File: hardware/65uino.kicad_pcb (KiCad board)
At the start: 2 copper layers, 74.9 x 53.3 mm, 57 parts, among them J1 Barrel_Jack_MountingPin, J2 USB_B_Micro, J3 OLED, SW1 RST, SW2 BTN, U1 R6507, U2 NC/74HC04, U3 6532, U4 w27C512, U5 MIC5504-3.3YM5, U6 LM1117-5.0, U7 SN74LVC1G14DBVR, X1 1MHz, Y1 NC/1Mhz

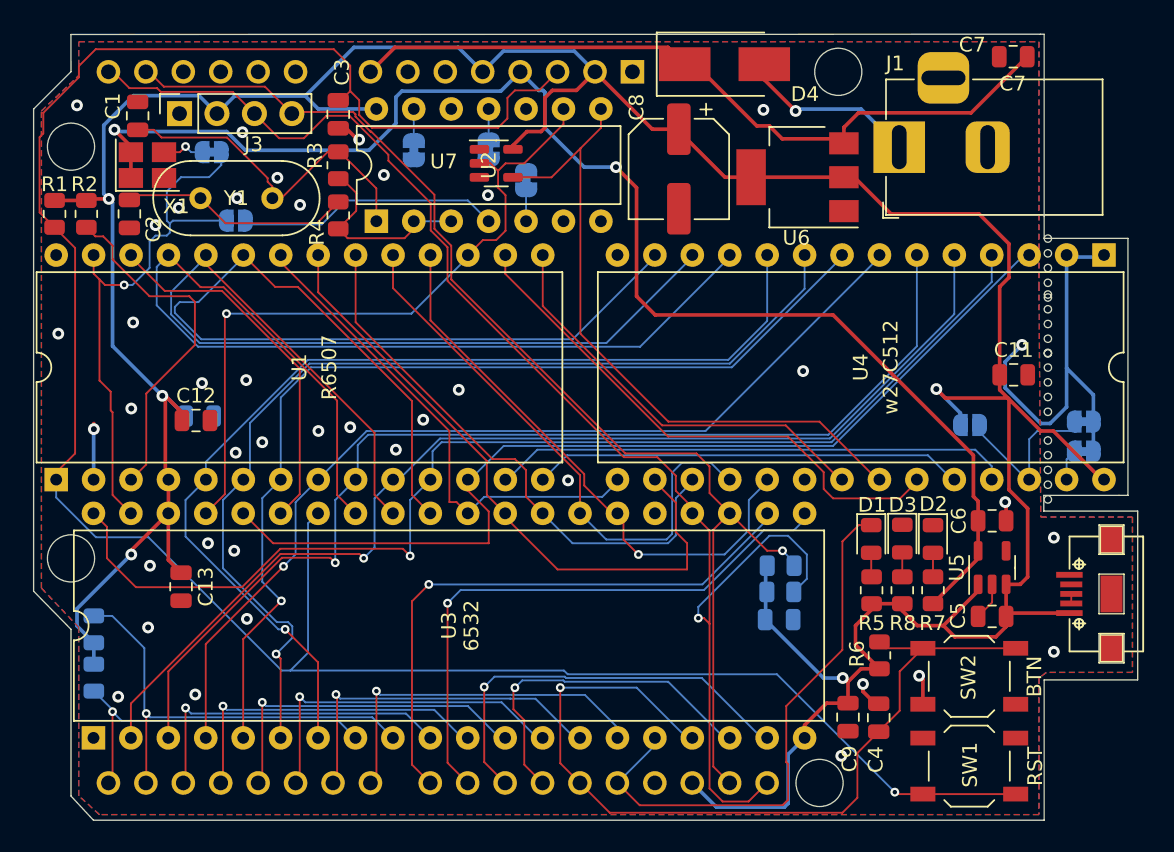
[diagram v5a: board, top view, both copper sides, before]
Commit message: Gerbers updated to match KiCAD
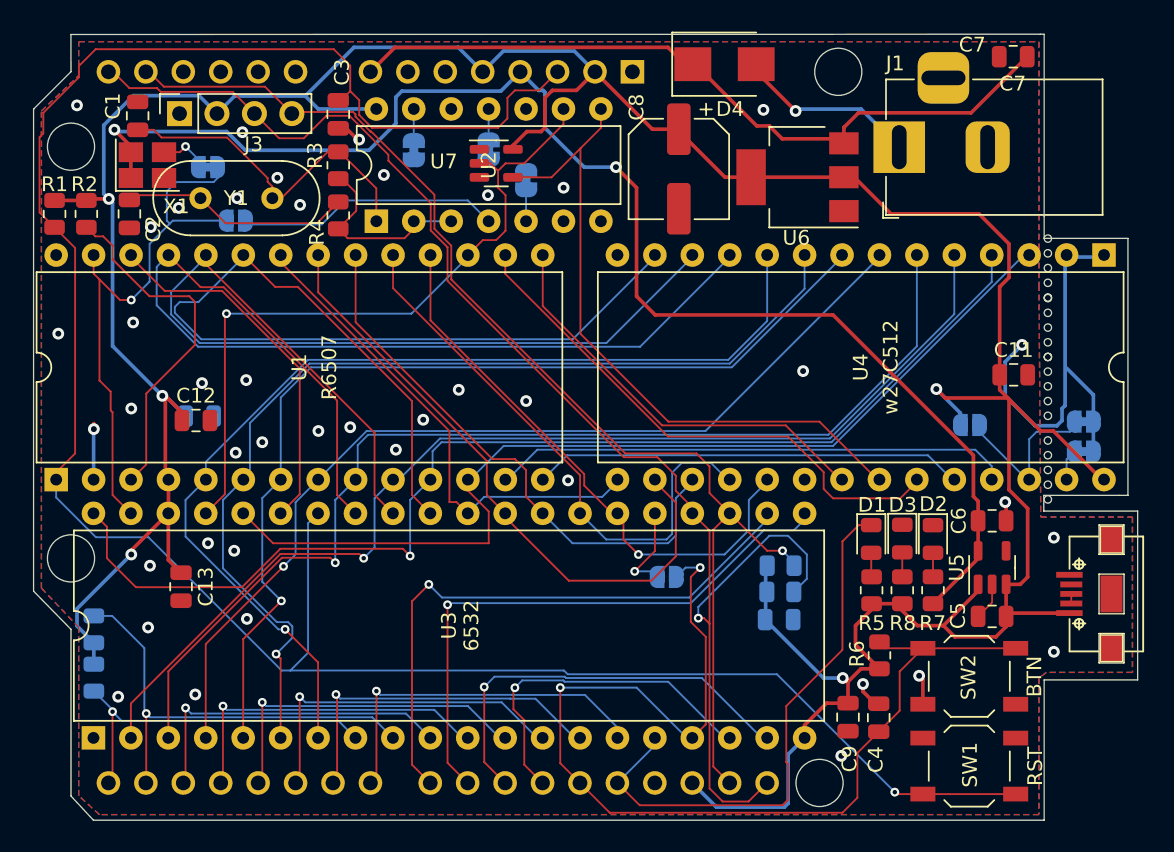
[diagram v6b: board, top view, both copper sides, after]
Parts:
- added JP9: SolderJumper_2_Bridged, Jumper:SolderJumper-2_P1.3mm_Open_RoundedPad1.0x1.5mm, B.Cu at (144.9, 85.3)
- D4: footprint Diode_SMD:D_SMB_Handsoldering -> Diode_SMD:D_SMB
- R10, R9: value 22k -> NC
- moved JP7 1.05 mm to (113.8, 57.5)
- moved REF** 0.27 mm to (170.8, 70.4)
- moved REF** 0.24 mm to (170.8, 66.4)
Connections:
- U3 pad 25: unconnected-(U3-Pad25) -> Net-(U3-Pad25)
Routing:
- net /PB6/D12: track 57.9 -> 72.4 mm, vias 1 -> 2
- net Net-(U3-Pad25): track 0.00 -> 6.19 mm, vias 0 -> 1
- net D4: track 43.5 -> 42.5 mm
- net GND: track 40.7 -> 41.6 mm, vias 40 -> 42
- net /PB2/D8: track 39.2 -> 40.0 mm
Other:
- board text added: "~{RW}"
- board text added: "Φ0"
- board text added: "Φ2 (NC)"
- board text removed: "PHI0"
